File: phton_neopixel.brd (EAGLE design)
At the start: 39 x 59.7 mm, 10 parts, among them J2 Neopixel, J3 POWER_JACK, U2 PHOTON_WITH_HEADERS

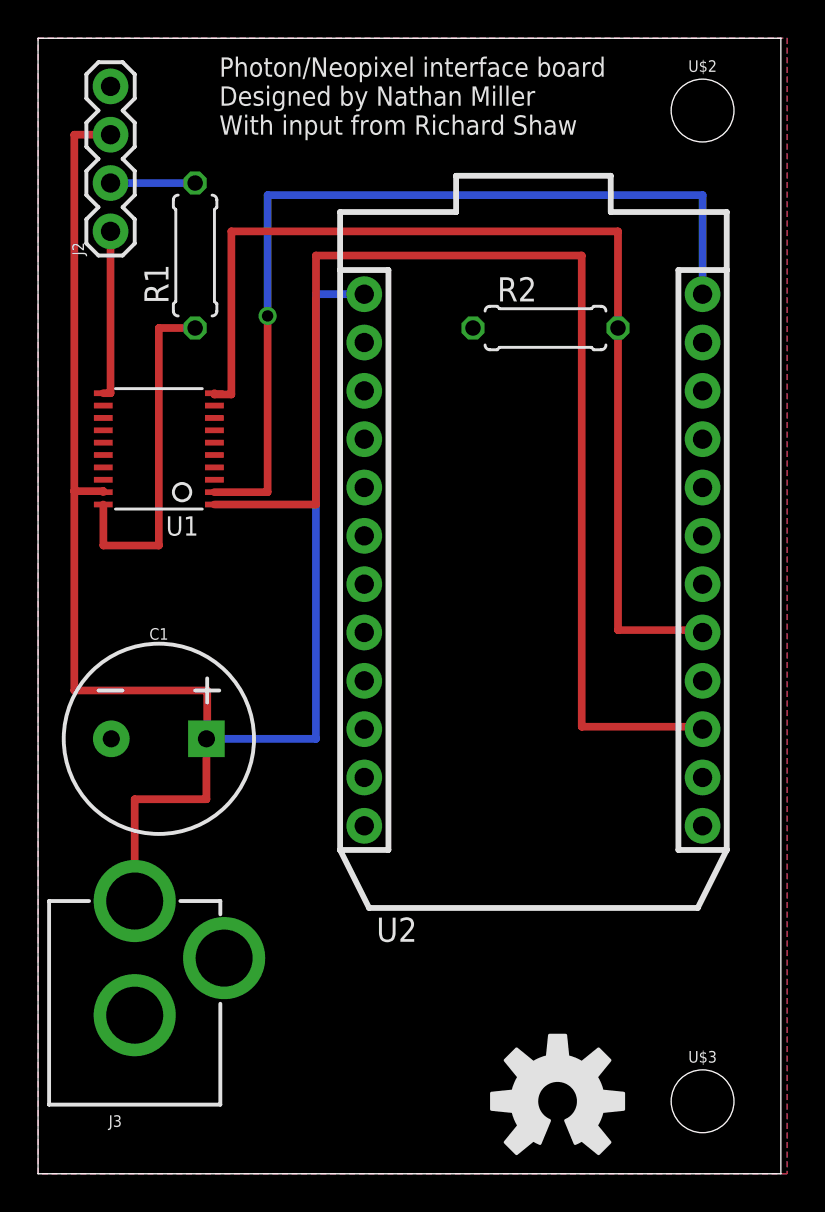
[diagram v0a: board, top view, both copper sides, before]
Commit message: Added filter caps and cleaned up the layout a lot
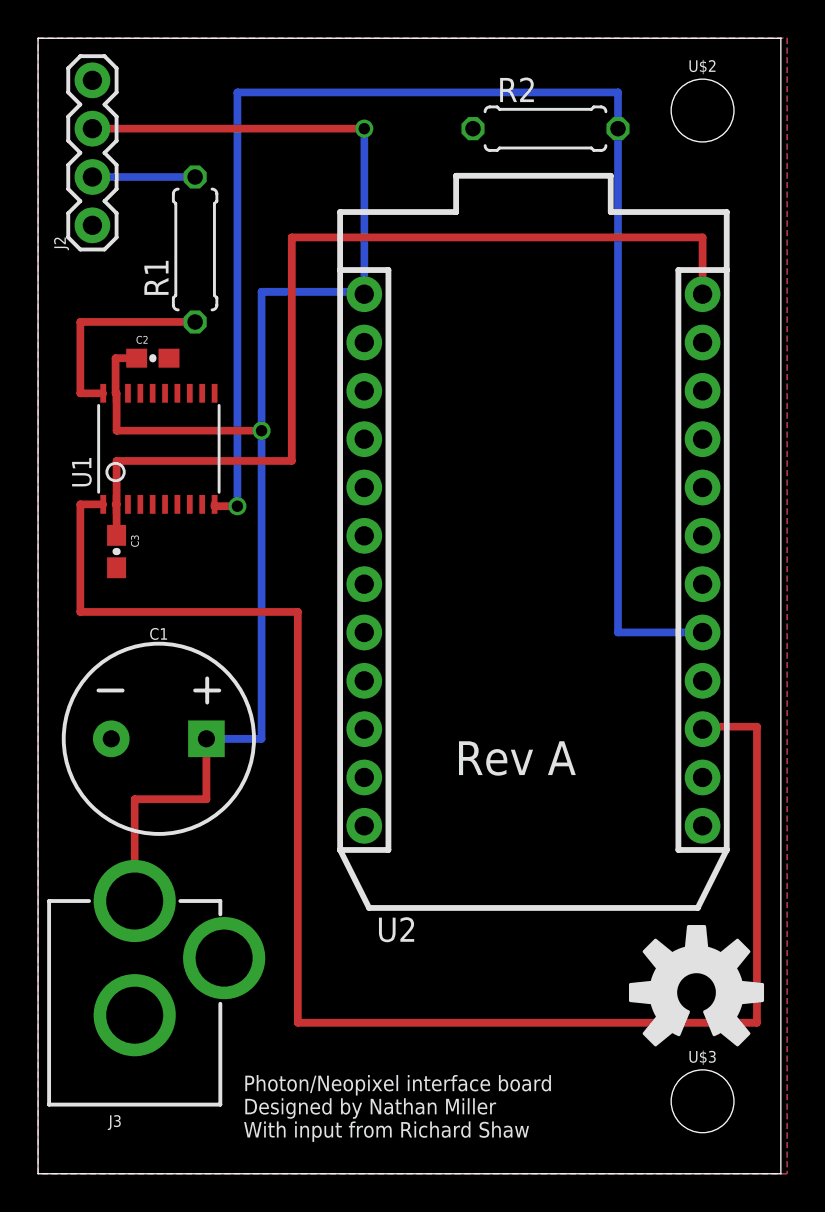
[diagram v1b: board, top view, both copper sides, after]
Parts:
- added C2, C3: 0.1uF, SparkFun-Capacitors:0603-CAP
- moved R2 10.5 mm to (26.7, 54.9)
- moved U$1 9.27 mm to (34.6, 9.53)
- moved J2 1.00 mm to (2.86, 49.8)
- moved R1 0.32 mm to (8.26, 48.6)
- turned U1 to 0 degrees
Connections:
- net 3.3V: now also C3.1
- net 5V: now also C2.1
- net GND: now also C2.2, C3.2
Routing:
- net N$3: track 55.4 -> 75.9 mm, vias 0 -> 1
- net N$5: track 63.6 -> 82.5 mm
- net GND: track 8.88 -> 0.00 mm
- net N$1: track 18.4 -> 11.0 mm
- net 5V: track 86.2 -> 80.2 mm, vias 0 -> 2
- net 3.3V: track 46.5 -> 49.5 mm, vias 1 -> 0
- net N$4: track 4.45 -> 5.40 mm
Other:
- board text added: "Rev A"
- board text added: "This side down."

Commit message: Added jumper for 5V to the photon, improved routing and naming
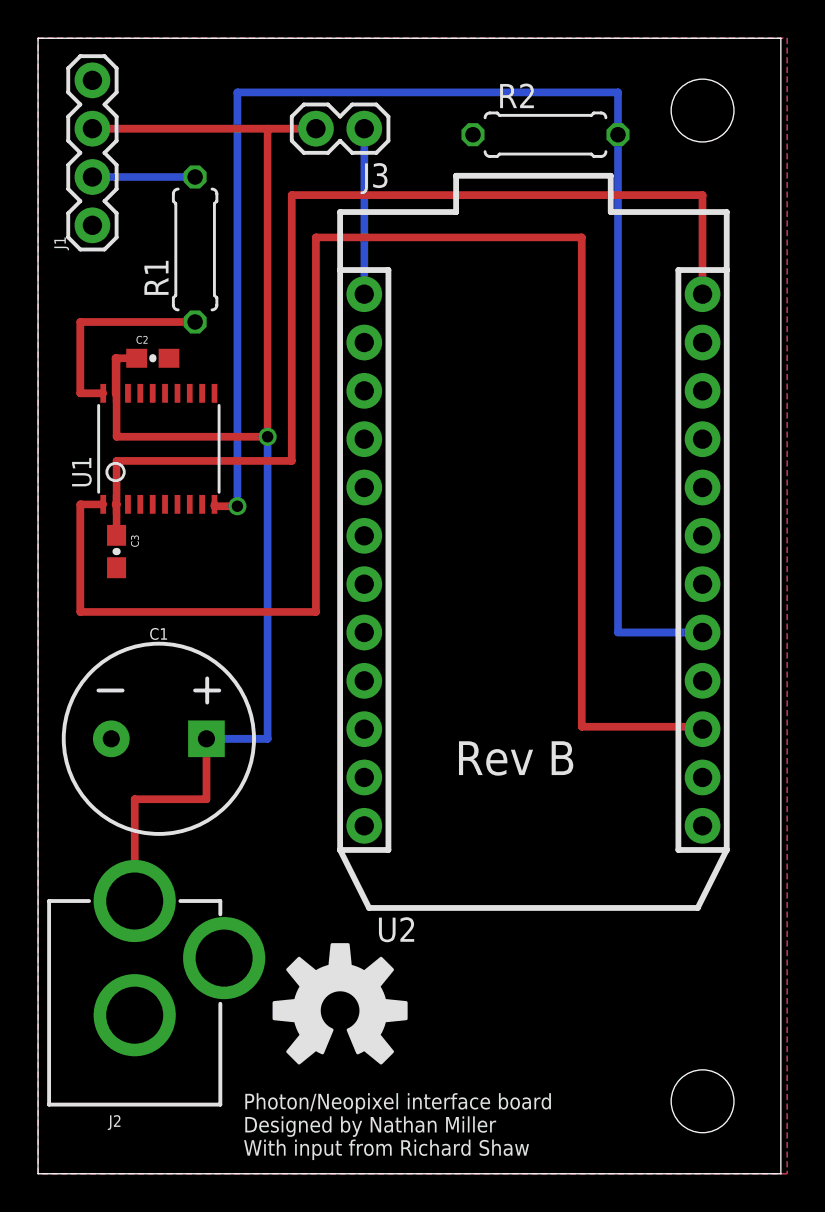
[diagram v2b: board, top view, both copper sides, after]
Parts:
- added J1: Neopixel, SparkFun-Connectors:1X04
- J2: value Neopixel -> POWER_JACK; device SparkFun-Connectors:1X04 -> SparkFun-Connectors:POWER_JACK_PTH
- J3: value POWER_JACK -> (none); device SparkFun-Connectors:POWER_JACK_PTH -> SparkFun-Connectors:1X02
- moved J3 55.6 mm to (17.1, 54.9), turned to 180 degrees
- moved J2 49.3 mm to (5.08, 0.64), turned to 0 degrees
- moved U$1 18.8 mm to (15.9, 8.57)
- moved R2 0.32 mm to (26.7, 54.6)
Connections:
- new net N$2: J3.1, U2.1
- net 5V: now also J1.3, J2.PWR, J3.2; no longer J2.3, J3.PWR, U2.1
- net GND: now also J1.1, J1.4, J2.GND, J2.GNDBREAK; no longer J2.1, J2.4, J3.GND, J3.GNDBREAK
- net N$4: now also J1.2; no longer J2.2
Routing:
- net N$2: track 0.00 -> 8.70 mm
- net 5V: track 80.2 -> 74.7 mm, vias 2 -> 1
- net 3.3V: track 49.5 -> 53.9 mm
- net N$5: track 82.5 -> 85.1 mm
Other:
- board text added: "Rev B"
- board text removed: "Rev A"
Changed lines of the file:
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@@
 <wire x1="39.04" y1="59.68" x2="0" y2="59.68" width="0" layer="20"/>
 <wire x1="0" y1="59.68" x2="0" y2="0" width="0" layer="20"/>
-<text x="10.795" y="1.905" size="0.8128" layer="21">Photon/Neopixel interface board
+<text x="10.795" y="0.9525" size="0.8128" layer="21">Photon/Neopixel interface board
 Designed by Nathan Miller
 With input from Richard Shaw</text>
@@
 <vertex x="17.145" y="17.145"/>
 </polygon>
-<text x="27.6225" y="1.905" size="1.778" layer="22" rot="MR0">This side down.</text>
-<text x="21.9075" y="20.955" size="1.778" layer="21">Rev A</text>
+<text x="27.6225" y="0.9525" size="1.778" layer="22" rot="MR0">This side down.</text>
+<text x="21.9075" y="20.955" size="1.778" layer="21">Rev B</text>
 </plain>
 <attributes>
@@
 <attribute name="PROD_ID" value="CAP-09538" x="6.35" y="22.86" size="1.778" layer="27" display="off"/>
 </element>
-<element name="J2" library="SparkFun-Connectors" package="1X04" value="Neopixel" x="2.8575" y="49.8475" rot="R90">
+<element name="J1" library="SparkFun-Connectors" package="1X04" value="Neopixel" x="2.8575" y="49.8475" rot="R90">
 <attribute name="PROD_ID" value="CONN-09696" x="2.8575" y="49.8475" size="1.778" layer="27" rot="R90" display="off"/>
 </element>
-<element name="J3" library="SparkFun-Connectors" package="POWER_JACK_PTH" value="POWER_JACK" x="5.08" y="0.635">
+<element name="J2" library="SparkFun-Connectors" package="POWER_JACK_PTH" value="POWER_JACK" x="5.08" y="0.635">
 <attribute name="PROD_ID" value="CONN-08197" x="5.08" y="0.635" size="1.778" layer="27" display="off"/>
 </element>
 <element name="R1" library="resistor" package="0207/7" value="470" x="8.255" y="48.5775" rot="R90"/>
-<element name="R2" library="resistor" package="0207/7" value="50k" x="26.67" y="54.9275"/>
+<element name="R2" library="resistor" package="0207/7" value="50k" x="26.67" y="54.61"/>
 <element name="U1" library="adafruit" package="TSSOP20" value="" x="6.35" y="38.1"/>
 <element name="U2" library="Spark" package="PHOTON" value="PHOTON_WITH_HEADERS" x="15.875" y="13.97" smashed="yes">
 <attribute name="NAME" x="17.78" y="12.192" size="1.27" layer="25" ratio="10"/>
 </element>
-<element name="U$1" library="SparkFun-Aesthetics" package="OSHW-LOGO-L" value="" x="34.6075" y="9.525"/>
-<element name="U$2" library="SparkFun-Hardware" package="STAND-OFF" value="" x="34.925" y="55.88"/>
-<element name="U$3" library="SparkFun-Hardware" package="STAND-OFF" value="" x="34.925" y="3.81"/>
+<element name="U$1" library="SparkFun-Aesthetics" package="OSHW-LOGO-L" value="" x="15.875" y="8.5725"/>
+<element name="U$2" library="SparkFun-Hardware" package="STAND-OFF" value="" x="34.925" y="55.88" smashed="yes">
+<attribute name="VALUE" x="34.925" y="53.848" size="0.6096" layer="27" font="vector" ratio="20" align="top-center"/>
+</element>
+<element name="U$3" library="SparkFun-Hardware" package="STAND-OFF" value="" x="34.925" y="3.81" smashed="yes">
+<attribute name="VALUE" x="34.925" y="1.778" size="0.6096" layer="27" font="vector" ratio="20" align="top-center"/>
+</element>
 <element name="C2" library="SparkFun-Capacitors" package="0603-CAP" value="0.1uF" x="6.0325" y="42.8625">
 <attribute name="PROD_ID" value="CAP-08604" x="6.0325" y="42.8625" size="1.778" layer="27" display="off"/>
@@
 <attribute name="PROD_ID" value="CAP-08604" x="4.1275" y="32.7025" size="1.778" layer="27" rot="R270" display="off"/>
 </element>
+<element name="J3" library="SparkFun-Connectors" package="1X02" value="" x="17.145" y="54.9275" rot="R180"/>
 </elements>
 <signals>
@@
 <contactref element="U2" pad="21"/>
 <contactref element="U1" pad="11"/>
-<contactref element="J2" pad="1"/>
-<contactref element="J2" pad="4"/>
+<contactref element="J1" pad="1"/>
+<contactref element="J1" pad="4"/>
 <contactref element="C1" pad="-"/>
 <contactref element="R2" pad="1"/>
-<contactref element="J3" pad="GND"/>
-<contactref element="J3" pad="GNDBREAK"/>
+<contactref element="J2" pad="GND"/>
+<contactref element="J2" pad="GNDBREAK"/>
 <polygon width="0.4064" layer="16">
 <vertex x="0" y="59.69"/>
@@
 <wire x1="4.1275" y1="35.1822" x2="4.1275" y2="37.465" width="0.4064" layer="1"/>
 <wire x1="4.1275" y1="37.465" x2="13.335" y2="37.465" width="0.4064" layer="1"/>
-<wire x1="13.335" y1="37.465" x2="13.335" y2="49.2125" width="0.4064" layer="1"/>
-<wire x1="13.335" y1="49.2125" x2="34.925" y2="49.2125" width="0.4064" layer="1"/>
-<wire x1="34.925" y1="49.2125" x2="34.925" y2="46.228" width="0.4064" layer="1"/>
+<wire x1="13.335" y1="37.465" x2="13.335" y2="51.435" width="0.4064" layer="1"/>
+<wire x1="13.335" y1="51.435" x2="34.925" y2="51.435" width="0.4064" layer="1"/>
+<wire x1="34.925" y1="51.435" x2="34.925" y2="46.228" width="0.4064" layer="1"/>
 </signal>
 <signal name="5V">
 <contactref element="U1" pad="19"/>
-<contactref element="J2" pad="3"/>
+<contactref element="J1" pad="3"/>
 <contactref element="C1" pad="+"/>
-<contactref element="J3" pad="PWR"/>
-<contactref element="U2" pad="1"/>
+<contactref element="J2" pad="PWR"/>
 <wire x1="5.08" y1="14.335" x2="5.08" y2="19.685" width="0.4064" layer="1"/>
 <wire x1="5.08" y1="19.685" x2="8.85" y2="19.685" width="0.4064" layer="1"/>
@@
 <contactref element="C2" pad="1"/>
 <wire x1="8.85" y1="22.86" x2="8.47" y2="22.86" width="0.4064" layer="1"/>
-<wire x1="5.1825" y1="42.8625" x2="4.075" y2="42.8625" width="0.4064" layer="1"/>
+<wire x1="5.1825" y1="42.8625" x2="4.1275" y2="42.8625" width="0.4064" layer="1"/>
 <wire x1="4.075" y1="42.8625" x2="4.075" y2="41.0178" width="0.4064" layer="1"/>
-<wire x1="4.075" y1="41.0178" x2="4.1275" y2="41.0178" width="0.4064" layer="1"/>
-<wire x1="4.1275" y1="41.0178" x2="4.1275" y2="39.0525" width="0.4064" layer="1"/>
-<wire x1="4.1275" y1="39.0525" x2="11.7475" y2="39.0525" width="0.4064" layer="1"/>
-<via x="11.7475" y="39.0525" extent="1-16" drill="0.6"/>
-<wire x1="11.7475" y1="39.0525" x2="11.7475" y2="46.355" width="0.4064" layer="16"/>
-<wire x1="11.7475" y1="46.355" x2="17.145" y2="46.355" width="0.4064" layer="16"/>
-<wire x1="17.145" y1="46.355" x2="17.145" y2="46.228" width="0.4064" layer="16"/>
-<wire x1="2.8575" y1="54.9275" x2="17.145" y2="54.9275" width="0.4064" layer="1"/>
-<via x="17.145" y="54.9275" extent="1-16" drill="0.6"/>
-<wire x1="17.145" y1="54.9275" x2="17.145" y2="46.228" width="0.4064" layer="16"/>
-<wire x1="8.85" y1="22.86" x2="11.7475" y2="22.86" width="0.4064" layer="16"/>
-<wire x1="11.7475" y1="22.86" x2="11.7475" y2="39.0525" width="0.4064" layer="16"/>
+<contactref element="J3" pad="2"/>
+<wire x1="2.8575" y1="54.9275" x2="12.065" y2="54.9275" width="0.4064" layer="1"/>
+<wire x1="12.065" y1="54.9275" x2="14.605" y2="54.9275" width="0.4064" layer="1"/>
+<wire x1="4.075" y1="42.8625" x2="4.1275" y2="42.8625" width="0.4064" layer="1"/>
+<wire x1="4.1275" y1="42.8625" x2="4.1275" y2="38.735" width="0.4064" layer="1"/>
+<wire x1="4.1275" y1="38.735" x2="12.065" y2="38.735" width="0.4064" layer="1"/>
+<wire x1="12.065" y1="38.735" x2="12.065" y2="54.9275" width="0.4064" layer="1"/>
+<via x="12.065" y="38.735" extent="1-16" drill="0.6"/>
+<wire x1="12.065" y1="38.735" x2="12.065" y2="22.86" width="0.4064" layer="16"/>
+<wire x1="12.065" y1="22.86" x2="8.85" y2="22.86" width="0.4064" layer="16"/>
 </signal>
 <signal name="N$4">
-<contactref element="J2" pad="2"/>
+<contactref element="J1" pad="2"/>
 <contactref element="R1" pad="2"/>
 <wire x1="8.255" y1="52.3875" x2="2.8575" y2="52.3875" width="0.4064" layer="16"/>
@@
 <contactref element="R2" pad="2"/>
 <contactref element="U2" pad="17"/>
-<wire x1="30.48" y1="54.9275" x2="30.48" y2="56.8325" width="0.4064" layer="16"/>
+<wire x1="30.48" y1="54.61" x2="30.48" y2="56.8325" width="0.4064" layer="16"/>
 <wire x1="30.48" y1="56.8325" x2="10.4775" y2="56.8325" width="0.4064" layer="16"/>
 <wire x1="10.4775" y1="56.8325" x2="10.4775" y2="35.08375" width="0.4064" layer="16"/>
@@
 <wire x1="9.275" y1="35.08375" x2="9.275" y2="35.1822" width="0.4064" layer="1"/>
 <wire x1="34.925" y1="28.448" x2="30.48" y2="28.448" width="0.4064" layer="16"/>
-<wire x1="30.48" y1="28.448" x2="30.48" y2="54.9275" width="0.4064" layer="16"/>
+<wire x1="30.48" y1="28.448" x2="30.48" y2="54.61" width="0.4064" layer="16"/>
 </signal>
 <signal name="N$1">
@@
 <wire x1="3.425" y1="35.1822" x2="2.2225" y2="35.1822" width="0.4064" layer="1"/>
 <wire x1="2.2225" y1="35.1822" x2="2.2225" y2="29.5275" width="0.4064" layer="1"/>
-<wire x1="2.2225" y1="29.5275" x2="13.6525" y2="29.5275" width="0.4064" layer="1"/>
-<wire x1="13.6525" y1="29.5275" x2="13.6525" y2="7.9375" width="0.4064" layer="1"/>
-<wire x1="13.6525" y1="7.9375" x2="37.7825" y2="7.9375" width="0.4064" layer="1"/>
-<wire x1="37.7825" y1="7.9375" x2="37.7825" y2="23.495" width="0.4064" layer="1"/>
-<wire x1="37.7825" y1="23.495" x2="34.925" y2="23.495" width="0.4064" layer="1"/>
+<wire x1="2.2225" y1="29.5275" x2="14.605" y2="29.5275" width="0.4064" layer="1"/>
+<wire x1="14.605" y1="29.5275" x2="14.605" y2="49.2125" width="0.4064" layer="1"/>
+<wire x1="14.605" y1="49.2125" x2="28.575" y2="49.2125" width="0.4064" layer="1"/>
+<wire x1="28.575" y1="49.2125" x2="28.575" y2="23.495" width="0.4064" layer="1"/>
+<wire x1="28.575" y1="23.495" x2="34.925" y2="23.495" width="0.4064" layer="1"/>
 <wire x1="34.925" y1="23.495" x2="34.925" y2="23.368" width="0.4064" layer="1"/>
 </signal>
+<signal name="N$2">
+<contactref element="J3" pad="1"/>
+<contactref element="U2" pad="1"/>
+<wire x1="17.145" y1="46.228" x2="17.145" y2="54.9275" width="0.4064" layer="16"/>
+</signal>
 </signals>
